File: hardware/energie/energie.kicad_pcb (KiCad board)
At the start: 2 copper layers, 102 x 87 mm, 94 parts, among them J1 transfos, J2 Conn_01x05_Pin, J3 linky, J4 Serial, J5 pilotes, J6 gpio, J7 I2C, J8 power, J9 ACin, Q1 BSS123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

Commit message: linky interface: update gate resitor value after tests
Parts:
- R13: value 10K -> 4.7k
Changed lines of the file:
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@@
 			)
 		)
-		(property "Value" "10K"
+		(property "Value" "4.7k"
 			(at 0 -1.65 180)
 			(layer "B.Fab")

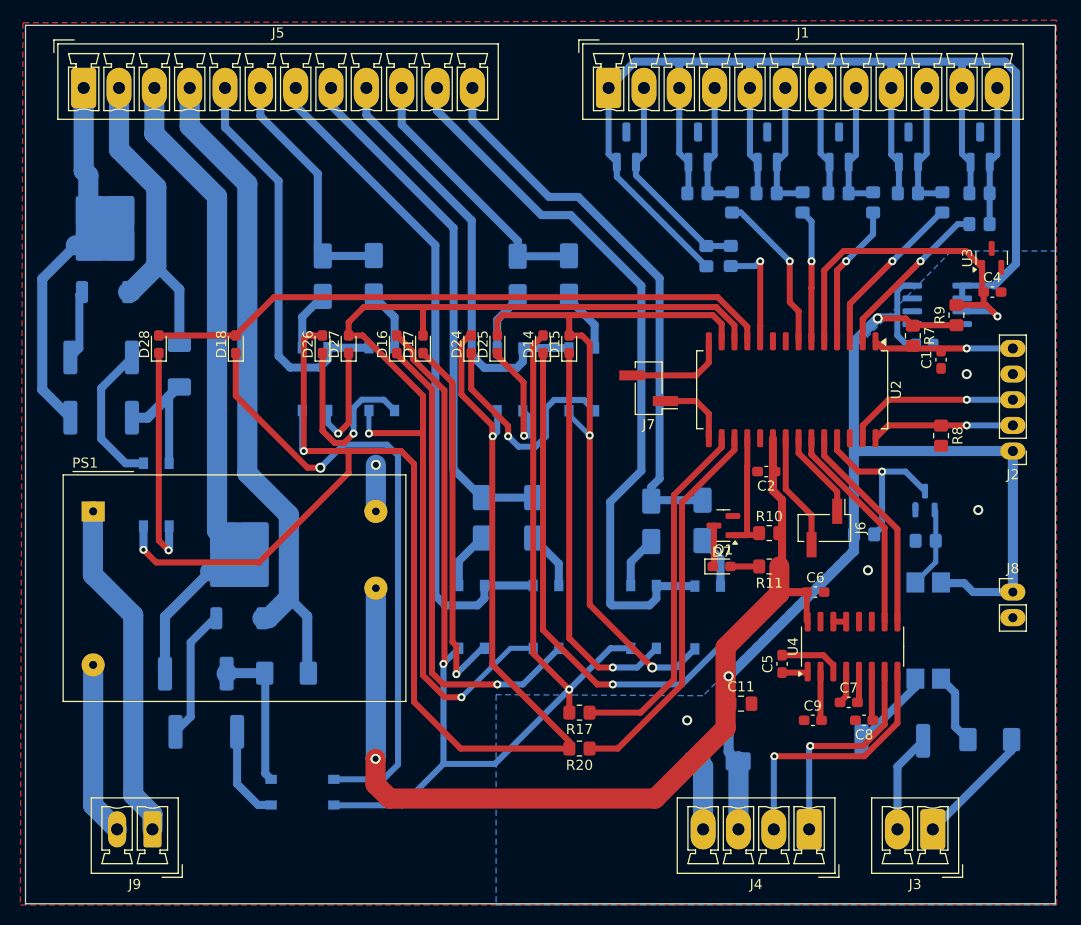
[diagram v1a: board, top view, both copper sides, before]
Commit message: energie: update PCB size to match casing
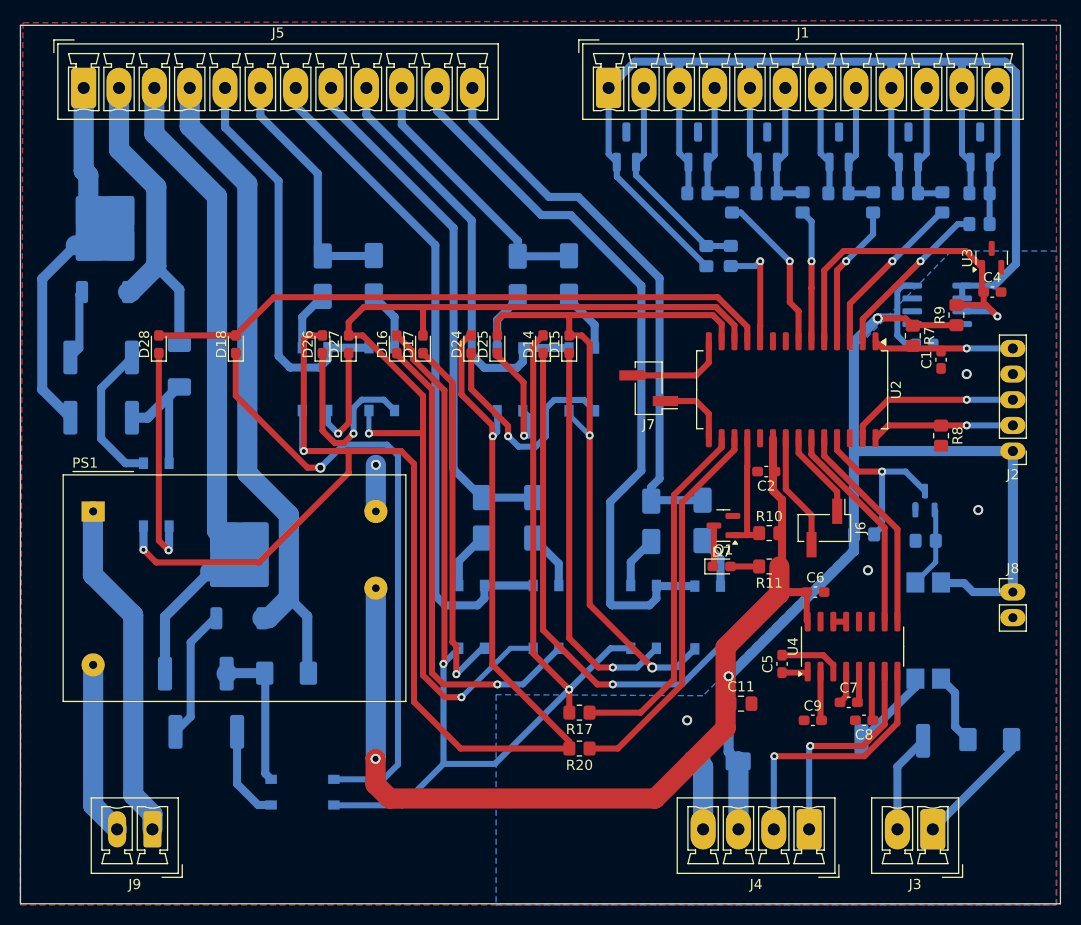
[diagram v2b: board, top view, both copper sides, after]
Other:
- board size 102 x 87 mm -> 103 x 87 mm
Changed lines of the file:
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@@
 	)
 	(gr_rect
-		(start 76.2 50.8)
-		(end 178.2 137.8)
+		(start 75.7 50.8)
+		(end 178.7 137.8)
 		(stroke
 			(width 0.05)

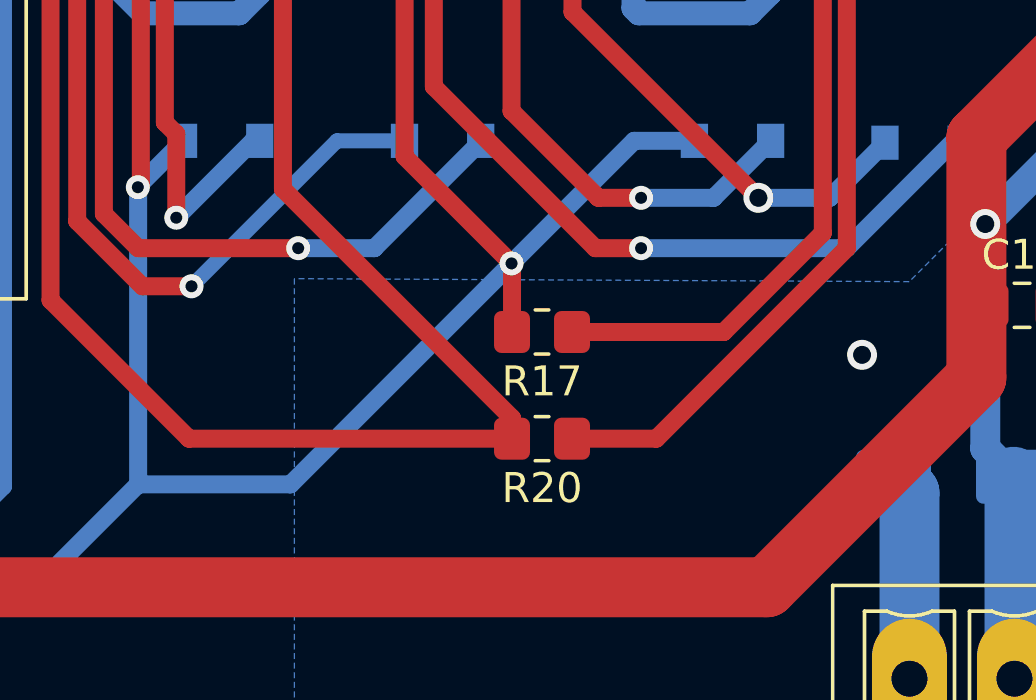
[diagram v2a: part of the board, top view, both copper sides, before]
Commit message: energie: ajout de zones interdites pour les supoort PCB du boitier.
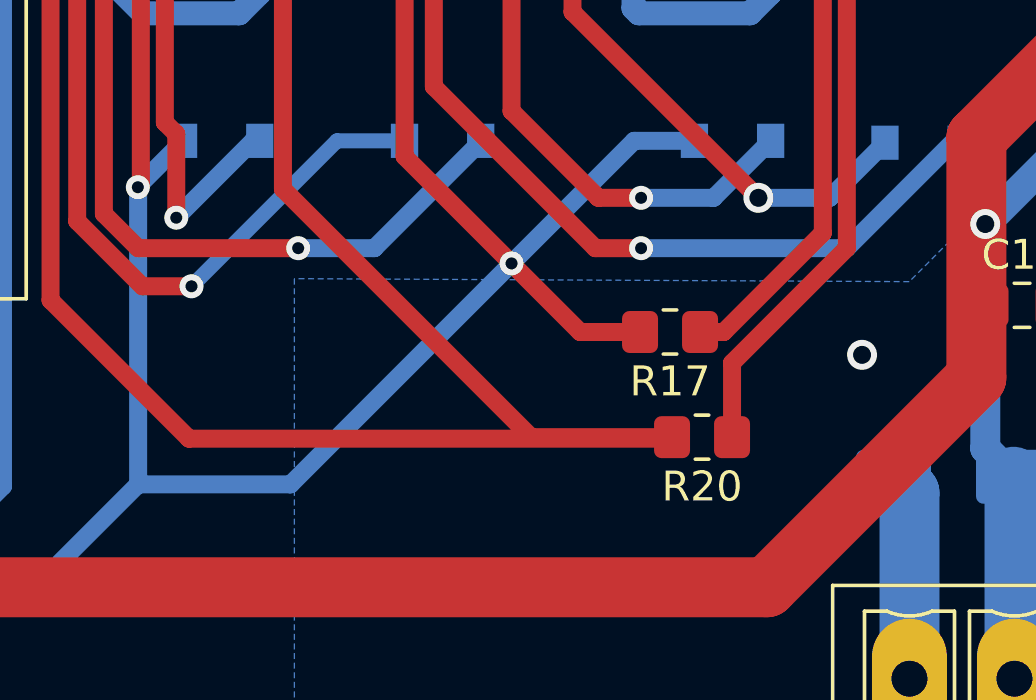
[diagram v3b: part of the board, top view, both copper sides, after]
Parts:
- moved R20 5.33 mm to (136.4, 122.4)
- moved R17 4.27 mm to (135.3, 118.9)
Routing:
- net Net-(D24-A): track 147.1 -> 157.2 mm
- net /outputs/O1: track 35.6 -> 31.3 mm
- net /outputs/O2: track 38.3 -> 34.4 mm
- net Net-(D14-A): track 121.4 -> 124.3 mm
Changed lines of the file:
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@@
 	(footprint "Resistor_SMD:R_0805_2012Metric_Pad1.20x1.40mm_HandSolder"
 		(layer "F.Cu")
-		(at 131.064 118.872 180)
+		(at 135.3312 118.872 180)
 		(descr "Resistor SMD 0805 (2012 Metric), square (rectangular) end terminal, IPC_7351 nominal with elongated pad for handsoldering. (Body size source: IPC-SM-782 page 72, https://www.pcb-3d.com/wordpress/wp-content/uploads/ipc-sm-782a_amendment_1_and_2.pdf), generated with kicad-footprint-generator")
 		(tags "resistor handsolder")
@@
 	(footprint "Resistor_SMD:R_0805_2012Metric_Pad1.20x1.40mm_HandSolder"
 		(layer "F.Cu")
-		(at 131.064 122.428 180)
+		(at 136.398 122.3772 180)
 		(descr "Resistor SMD 0805 (2012 Metric), square (rectangular) end terminal, IPC_7351 nominal with elongated pad for handsoldering. (Body size source: IPC-SM-782 page 72, https://www.pcb-3d.com/wordpress/wp-content/uploads/ipc-sm-782a_amendment_1_and_2.pdf), generated with kicad-footprint-generator")
 		(tags "resistor handsolder")
@@
 	)
 	(segment
-		(start 122.428 114.1055)
-		(end 130.064 121.7415)
+		(start 119.29663 122.428)
+		(end 114.681 117.81237)
 		(width 0.6)
 		(layer "F.Cu")
@@
 	)
 	(segment
-		(start 119.29663 122.428)
-		(end 114.681 117.81237)
-		(width 0.6)
-		(layer "F.Cu")
-		(net 37)
-	)
-	(segment
-		(start 122.428 90.424)
-		(end 122.428 114.1055)
-		(width 0.6)
-		(layer "F.Cu")
-		(net 37)
-	)
-	(segment
 		(start 120.159 81.517)
 		(end 119.371 82.305)
@@
 	)
 	(segment
-		(start 130.064 122.428)
-		(end 119.29663 122.428)
+		(start 113.409 92.962)
+		(end 108.204 92.962)
 		(width 0.6)
 		(layer "F.Cu")
@@
 	)
 	(segment
-		(start 113.409 92.962)
-		(end 108.204 92.962)
+		(start 130.6997 122.3772)
+		(end 135.398 122.3772)
+		(width 0.6)
+		(layer "F.Cu")
+		(net 37)
+	)
+	(segment
+		(start 122.428 90.424)
+		(end 122.428 114.1055)
 		(width 0.6)
 		(layer "F.Cu")
@@
 	)
 	(segment
-		(start 119.371 87.367)
-		(end 122.428 90.424)
+		(start 108.204 95.123)
+		(end 108.204 92.962)
 		(width 0.6)
 		(layer "F.Cu")
@@
 	)
 	(segment
-		(start 108.204 95.123)
-		(end 108.204 92.962)
+		(start 114.681 94.234)
+		(end 113.409 92.962)
 		(width 0.6)
 		(layer "F.Cu")
@@
 	)
 	(segment
-		(start 130.064 121.7415)
-		(end 130.064 122.428)
+		(start 119.371 82.305)
+		(end 119.371 87.367)
 		(width 0.6)
 		(layer "F.Cu")
@@
 	)
 	(segment
-		(start 114.681 94.234)
-		(end 113.409 92.962)
+		(start 119.371 87.367)
+		(end 122.428 90.424)
 		(width 0.6)
 		(layer "F.Cu")
@@
 	)
 	(segment
-		(start 119.371 82.305)
-		(end 119.371 87.367)
+		(start 122.428 114.1055)
+		(end 130.6997 122.3772)
 		(width 0.6)
 		(layer "F.Cu")
@@
 		(net 37)
 	)
+	(segment
+		(start 135.3472 122.428)
+		(end 119.29663 122.428)
+		(width 0.6)
+		(layer "F.Cu")
+		(net 37)
+	)
 	(via
 		(at 103.759 92.962)
@@
 	)
 	(segment
-		(start 145.147 92.593999)
-		(end 140.424 97.316999)
-		(width 0.6)
-		(layer "F.Cu")
-		(net 42)
-	)
-	(segment
 		(start 137.122 118.872)
-		(end 132.064 118.872)
+		(end 136.3312 118.872)
 		(width 0.6)
 		(layer "F.Cu")
@@
 	)
 	(segment
-		(start 140.424 115.57)
-		(end 137.122 118.872)
+		(start 140.424 97.316999)
+		(end 140.424 115.57)
 		(width 0.6)
 		(layer "F.Cu")
@@
 	)
 	(segment
-		(start 140.424 97.316999)
-		(end 140.424 115.57)
+		(start 145.147 91.694)
+		(end 145.147 92.593999)
 		(width 0.6)
 		(layer "F.Cu")
@@
 	)
 	(segment
-		(start 145.147 91.694)
-		(end 145.147 92.593999)
+		(start 145.147 92.593999)
+		(end 140.424 97.316999)
 		(width 0.6)
 		(layer "F.Cu")
@@
 	)
 	(segment
-		(start 141.224 98.044)
-		(end 141.224 116.078)
+		(start 140.424 115.57)
+		(end 137.122 118.872)
 		(width 0.6)
 		(layer "F.Cu")
-		(net 43)
+		(net 42)
 	)
 	(segment
@@
 	)
 	(segment
-		(start 134.874 122.428)
-		(end 132.064 122.428)
+		(start 141.224 98.044)
+		(end 141.224 116.078)
 		(width 0.6)
 		(layer "F.Cu")
@@
 	(segment
 		(start 141.224 116.078)
-		(end 134.874 122.428)
+		(end 137.398 119.904)
+		(width 0.6)
+		(layer "F.Cu")
+		(net 43)
+	)
+	(segment
+		(start 137.398 119.904)
+		(end 137.398 122.3772)
 		(width 0.6)
 		(layer "F.Cu")
@@
 	)
 	(segment
-		(start 126.483 82.492)
-		(end 126.483 113.021)
+		(start 134.3312 118.872)
+		(end 132.334 118.872)
 		(width 0.6)
 		(layer "F.Cu")
@@
 	)
 	(segment
-		(start 126.483 113.021)
-		(end 130.048 116.586)
+		(start 126.483 82.492)
+		(end 126.483 113.021)
 		(width 0.6)
 		(layer "F.Cu")
@@
 	)
 	(segment
-		(start 130.064 116.602)
+		(start 126.483 113.021)
 		(end 130.048 116.586)
 		(width 0.6)
@@
 	)
 	(segment
-		(start 117.691 113.946)
-		(end 117.691 86.962564)
+		(start 132.334 118.872)
+		(end 130.048 116.586)
 		(width 0.6)
 		(layer "F.Cu")
@@
 	)
 	(segment
-		(start 127.458 81.517)
-		(end 126.483 82.492)
+		(start 117.691 113.946)
+		(end 117.691 86.962564)
 		(width 0.6)
 		(layer "F.Cu")
@@
 	)
 	(segment
-		(start 130.064 118.872)
-		(end 130.064 116.602)
+		(start 127.458 81.517)
+		(end 126.483 82.492)
 		(width 0.6)
 		(layer "F.Cu")
@@
 		(keepout
 			(tracks allowed)
+			(vias not_allowed)
+			(pads not_allowed)
+			(copperpour allowed)
+			(footprints not_allowed)
+		)
+		(fill
+			(thermal_gap 0.5)
+			(thermal_bridge_width 0.5)
+		)
+		(polygon
+			(pts
+				(xy 123.2 123.8) (xy 131.2 123.8) (xy 131.2 125.8) (xy 123.2 125.8)
+			)
+		)
+	)
+	(zone
+		(net 0)
+		(net_name "")
+		(layer "F.Cu")
+		(hatch edge 0.5)
+		(connect_pads
+			(clearance 0)
+		)
+		(min_thickness 0.25)
+		(filled_areas_thickness no)
+		(keepout
+			(tracks allowed)
 			(vias allowed)
 			(pads allowed)
@@
 			)
 		)
+	)
+	(zone
+		(net 0)
+		(net_name "")
+		(layer "F.Cu")
+		(hatch edge 0.5)
+		(connect_pads
+			(clearance 0)
+		)
+		(min_thickness 0.25)
+		(filled_areas_thickness no)
+		(keepout
+			(tracks allowed)
+			(vias not_allowed)
+			(pads not_allowed)
+			(copperpour allowed)
+			(footprints not_allowed)
+		)
+		(fill
+			(thermal_gap 0.5)
+			(thermal_bridge_width 0.5)
+		)
+		(polygon
+			(pts
+				(xy 123.2 62.8) (xy 131.2 62.8) (xy 131.2 64.8) (xy 123.2 64.8)
+			)
+		)

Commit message: energie: name rs232_RX/TX
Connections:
- net Net-(J4-Pin_1) renamed /rs232_TX
- net Net-(J4-Pin_2) renamed /rs232_RX
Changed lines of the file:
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@@
 	(net 2 "Net-(J5-Pin_5)")
 	(net 3 "+5V")
-	(net 4 "Net-(J4-Pin_1)")
+	(net 4 "/rs232_RX")
 	(net 5 "Vref")
 	(net 6 "Net-(C12-Pad2)")
@@
 	(net 39 "PGD")
 	(net 40 "Net-(Q1-G)")
-	(net 41 "Net-(J4-Pin_2)")
+	(net 41 "/rs232_TX")
 	(net 42 "/outputs/O1")
 	(net 43 "/outputs/O2")
@@
 			(remove_unused_layers no)
 			(roundrect_rratio 0.138889)
-			(net 4 "Net-(J4-Pin_1)")
+			(net 41 "/rs232_TX")
 			(pinfunction "Pin_1")
 			(pintype "passive")
@@
 			(layers "*.Cu" "*.Mask")
 			(remove_unused_layers no)
-			(net 41 "Net-(J4-Pin_2)")
+			(net 4 "/rs232_RX")
 			(pinfunction "Pin_2")
 			(pintype "passive")
@@
 			(layers "F.Cu" "F.Paste" "F.Mask")
 			(roundrect_rratio 0.25)
-			(net 4 "Net-(J4-Pin_1)")
+			(net 41 "/rs232_TX")
 			(pinfunction "T2OUT")
 			(pintype "output")
@@
 			(layers "F.Cu" "F.Paste" "F.Mask")
 			(roundrect_rratio 0.25)
-			(net 41 "Net-(J4-Pin_2)")
+			(net 4 "/rs232_RX")
 			(pinfunction "R2IN")
 			(pintype "input")
@@
 	)
 	(segment
-		(start 161.29 120.051564)
-		(end 161.29 114.808)
+		(start 159.282935 123.19)
+		(end 150.368 123.19)
 		(width 0.6)
 		(layer "F.Cu")
@@
 	)
 	(segment
-		(start 153.924 122.174)
-		(end 159.167564 122.174)
+		(start 162.56 114.808)
+		(end 162.56 119.912935)
 		(width 0.6)
 		(layer "F.Cu")
@@
 	)
 	(segment
-		(start 159.167564 122.174)
-		(end 161.29 120.051564)
+		(start 162.56 119.912935)
+		(end 159.282935 123.19)
 		(width 0.6)
 		(layer "F.Cu")
@@
 	)
 	(via
-		(at 153.924 122.174)
+		(at 150.368 123.19)
 		(size 0.8)
 		(drill 0.4)
@@
 	)
 	(segment
-		(start 153.812 122.286)
-		(end 153.812 130.429)
+		(start 150.312 123.246)
+		(end 150.312 130.429)
 		(width 0.6)
 		(layer "B.Cu")
@@
 	)
 	(segment
-		(start 153.924 122.174)
-		(end 153.812 122.286)
+		(start 150.368 123.19)
+		(end 150.312 123.246)
 		(width 0.6)
 		(layer "B.Cu")
@@
 	)
 	(segment
-		(start 159.282935 123.19)
-		(end 150.368 123.19)
+		(start 161.29 120.051564)
+		(end 161.29 114.808)
 		(width 0.6)
 		(layer "F.Cu")
@@
 	)
 	(segment
-		(start 162.56 114.808)
-		(end 162.56 119.912935)
+		(start 153.924 122.174)
+		(end 159.167564 122.174)
 		(width 0.6)
 		(layer "F.Cu")
@@
 	)
 	(segment
-		(start 162.56 119.912935)
-		(end 159.282935 123.19)
+		(start 159.167564 122.174)
+		(end 161.29 120.051564)
 		(width 0.6)
 		(layer "F.Cu")
@@
 	)
 	(via
-		(at 150.368 123.19)
+		(at 153.924 122.174)
 		(size 0.8)
 		(drill 0.4)
@@
 	)
 	(segment
-		(start 150.312 123.246)
-		(end 150.312 130.429)
+		(start 153.812 122.286)
+		(end 153.812 130.429)
 		(width 0.6)
 		(layer "B.Cu")
@@
 	)
 	(segment
-		(start 150.368 123.19)
-		(end 150.312 123.246)
+		(start 153.924 122.174)
+		(end 153.812 122.286)
 		(width 0.6)
 		(layer "B.Cu")
